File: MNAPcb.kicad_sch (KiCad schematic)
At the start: 10 parts, among them J1 STLINK/V2, J2 DA15_Socket, J3 USB_C_Receptacle_USB2.0_16P, J4 Conn_Coaxial, J5 SineWaveIn1, J6 SineWaveIn, J7 Conn_01x02

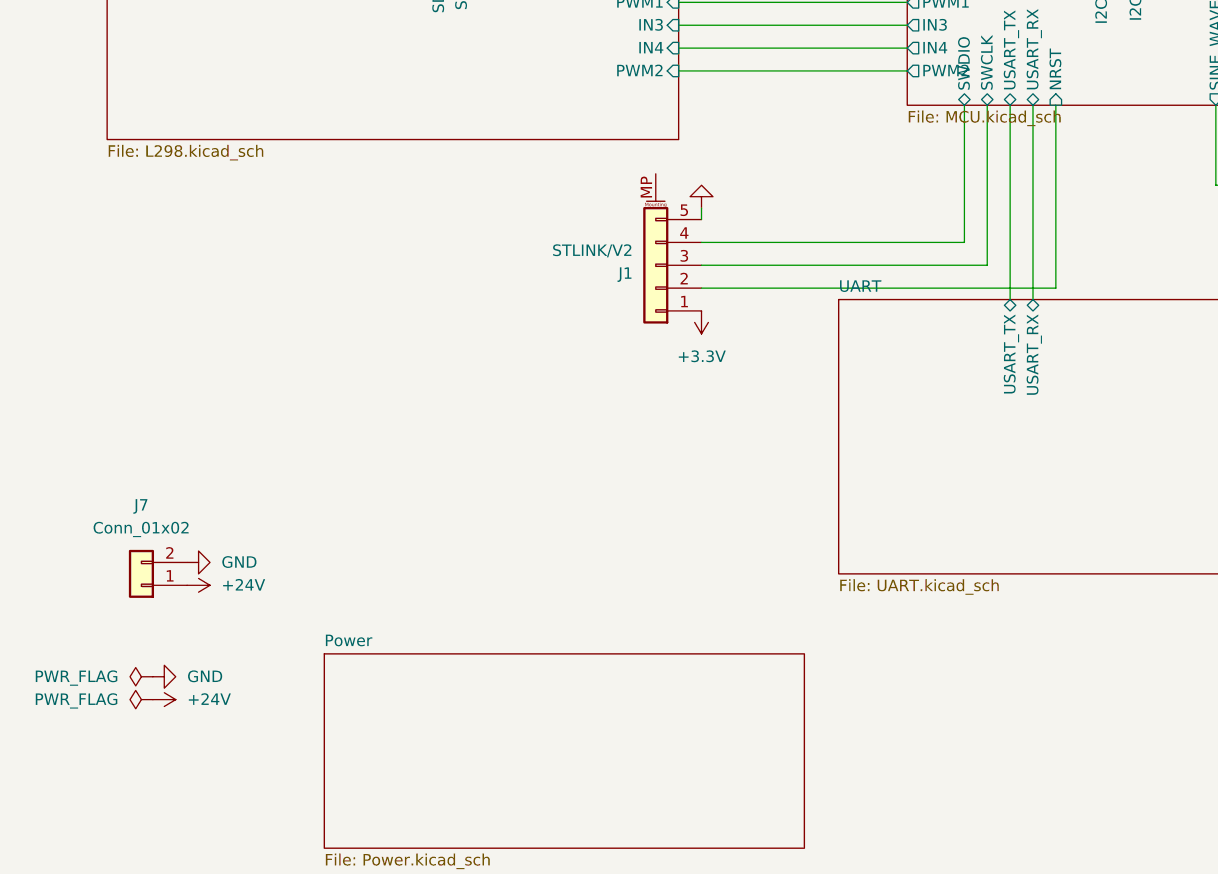
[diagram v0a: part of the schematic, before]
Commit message: Added Footprint
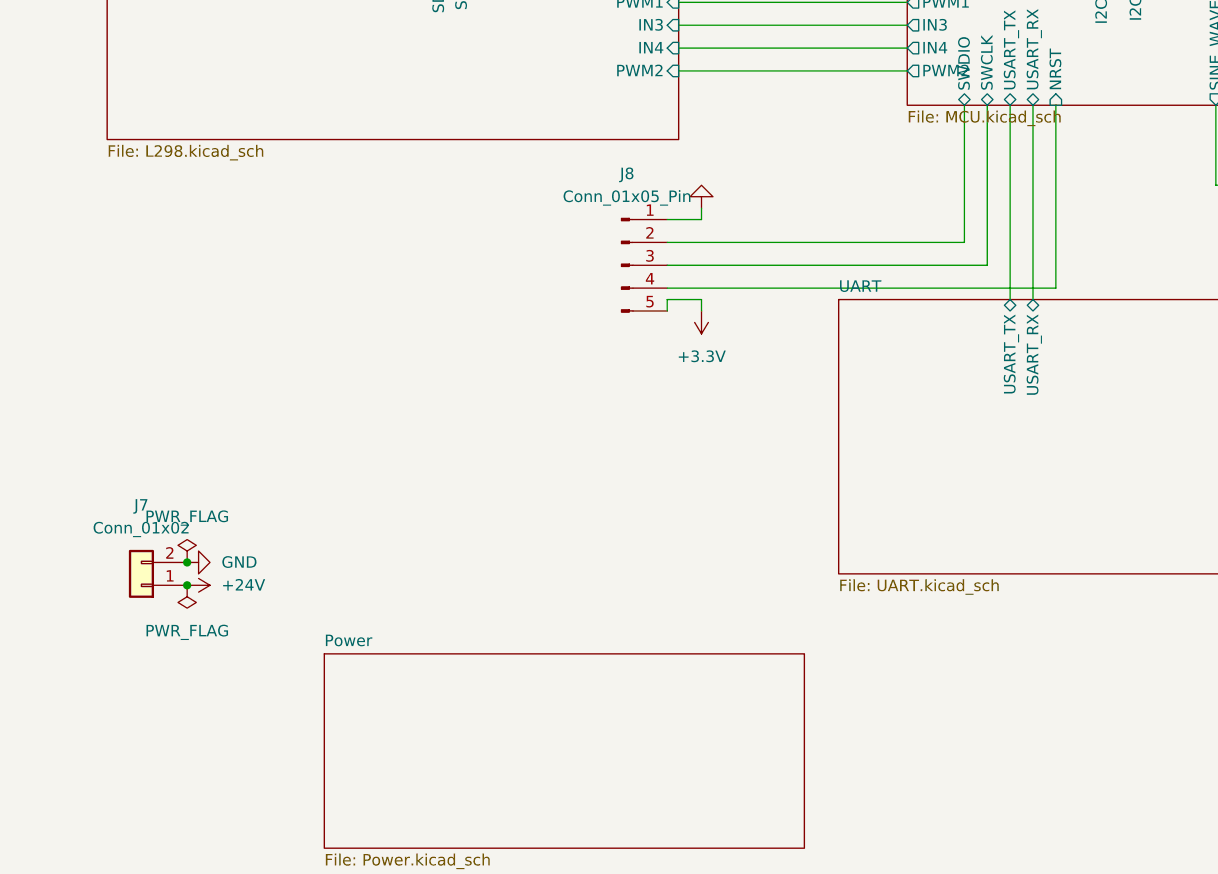
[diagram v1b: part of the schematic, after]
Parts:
- removed J1: STLINK/V2, symbol Connector_Generic_MountingPin:Conn_01x05_MountingPin
- added J8: Conn_01x05_Pin, Connector_PinHeader_2.54mm:PinHeader_1x05_P2.54mm_Vertical_SMD_Pin1Left, symbol Connector:Conn_01x05_Pin
- C17: footprint (none) -> Capacitor_SMD:C_0805_2012Metric_Pad1.18x1.45mm_HandSolder
- J3: footprint (none) -> Connector_USB:USB_C_Receptacle_HRO_TYPE-C-31-M-12
- R10, R7: footprint (none) -> Resistor_SMD:R_0805_2012Metric_Pad1.20x1.40mm_HandSolder
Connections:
- net +3.3V: now also J8.5 (Pin_5)
- net GND: now also J8.1 (Pin_1)
- net MCU/NRST: now also J8.4 (Pin_4)
- net MCU/SWCLK: now also J8.3 (Pin_3)
- net MCU/SWDIO: now also J8.2 (Pin_2)

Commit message: Added a Relay Circuit
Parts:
- added J1: DA15_Socket, Connector_Dsub:DSUB-15_Socket_Horizontal_P2.77x2.54mm_EdgePinOffset9.40mm, symbol Connector:DA15_Socket
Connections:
- no-connect marks 8 -> 14
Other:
- added sheet RelayControl (RelayControl.kicad_sch)
- sheet MCU ports: added K1IN, K2IN, K3IN, K4IN; removed none
- moved on the sheet: J4, J5, J6

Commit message: Solved errors
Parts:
- removed J1: DA15_Socket, Connector_Dsub:DSUB-15_Socket_Horizontal_P2.77x2.54mm_EdgePinOffset9.40mm, symbol Connector:DA15_Socket
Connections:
- net RelayControl/K1OUT: now also J2.6
- net RelayControl/K2OUT: now also J2.15 (P15)
- net RelayControl/K3OUT: now also J2.14 (P14)
- net RelayControl/K4OUT: now also J2.13 (P13)
- no-connect marks 14 -> 4
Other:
- sheet RelayControl ports: added none; removed SCL_RELAY, SDA_RELAY

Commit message: New PCB Changes
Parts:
- J7: footprint (none) -> Connector_TE-Connectivity:TE_826576-2_1x02_P3.96mm_Vertical
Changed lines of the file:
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@@
 			)
 		)
-		(property "Footprint" ""
+		(property "Footprint" "Connector_TE-Connectivity:TE_826576-2_1x02_P3.96mm_Vertical"
 			(at 19.05 138.43 0)
 			(effects

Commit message: FInal Changes in Schgematic
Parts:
- removed J5: SineWaveIn1, Connector_Coaxial:SMA_Amphenol_132289_EdgeMount, symbol Connector:Conn_Coaxial
- added H1, H2, H3, H4: MountingHole, MountingHole:MountingHole_3.2mm_M3_DIN965, symbol Mechanical:MountingHole
- added J1: Conn_01x03_Pin, Connector_Molex:Molex_KK-254_AE-6410-03A_1x03_P2.54mm_Vertical, symbol Connector:Conn_01x03_Pin
- added J5, J9: Conn_01x02, Connector_TE-Connectivity:TE_826576-2_1x02_P3.96mm_Vertical, symbol Connector_Generic:Conn_01x02
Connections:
- net GND: now also J1.2 (Pin_2), J5.1 (Pin_1), J9.1 (Pin_1)
- net +3.3V: no longer names the net of J8.5 (Pin_5)
- new net +12: J5.2 (Pin_2)
- new net +15: J1.1 (Pin_1)
- new net +24: J9.2 (Pin_2)
- new net -15V: J1.3 (Pin_3)
- no-connect marks 4 -> 5
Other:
- added sheet CurrentTracking (untitled.kicad_sch)
- sheet L298 ports: added none; removed SCL_MOTOR, SDA_MOTOR

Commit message: Fixed the Silkscreen issue
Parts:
- J3: footprint Connector_USB:USB_C_Receptacle_HRO_TYPE-C-31-M-12 -> Connector_USB:USB_C_Receptacle_GCT_USB4085
- J8: footprint Connector_PinHeader_2.54mm:PinHeader_1x05_P2.54mm_Vertical_SMD_Pin1Left -> Connector_PinHeader_2.54mm:PinHeader_1x05_P2.54mm_Vertical
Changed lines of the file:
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@@
 			)
 		)
-		(property "Footprint" "Connector_USB:USB_C_Receptacle_HRO_TYPE-C-31-M-12"
+		(property "Footprint" "Connector_USB:USB_C_Receptacle_GCT_USB4085"
 			(at 219.71 120.65 0)
 			(effects
@@
 			)
 		)
-		(property "Footprint" "Connector_PinHeader_2.54mm:PinHeader_1x05_P2.54mm_Vertical_SMD_Pin1Left"
+		(property "Footprint" "Connector_PinHeader_2.54mm:PinHeader_1x05_P2.54mm_Vertical"
 			(at 72.39 102.87 0)
 			(effects

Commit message: Deleted Uneeded Portion
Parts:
- removed J4: Conn_Coaxial, Connector_Coaxial:SMA_Amphenol_132289_EdgeMount, symbol Connector:Conn_Coaxial
- removed J6: SineWaveIn, Connector_Coaxial:SMA_Amphenol_132289_EdgeMount, symbol Connector:Conn_Coaxial
- removed J8: Conn_01x05_Pin, Connector_PinHeader_2.54mm:PinHeader_1x05_P2.54mm_Vertical, symbol Connector:Conn_01x05_Pin
- added J8: Conn_01x04_Pin, Connector_JST:JST_EH_B4B-EH-A_1x04_P2.50mm_Vertical, symbol Connector:Conn_01x04_Pin
- J3: footprint Connector_USB:USB_C_Receptacle_GCT_USB4085 -> Connector_USB:USB_C_Receptacle_G-Switch_GT-USB-7010ASV
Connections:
- net RelayControl/K2OUT is gone; now on net ADC/POT2_V: J2.15 (P15)
- net +12: now also J2.8
- net ADC/POT1_V: now also J2.7; no longer J2.5
- net ADC/POT2_V: no longer J2.12 (P12)
- net GND: now also J8.4 (Pin_4)
- net MCU/NRST: now also J8.1 (Pin_1)
- net MCU/SWCLK: now also J8.2 (Pin_2)
- net MCU/SWDIO: now also J8.3 (Pin_3)
- net +12V: no longer names the net of J2.4
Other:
- sheet ADC ports: added none; removed ADC2, SineWaveIn
- sheet MCU ports: added none; removed ADC2, SINE_WAVE

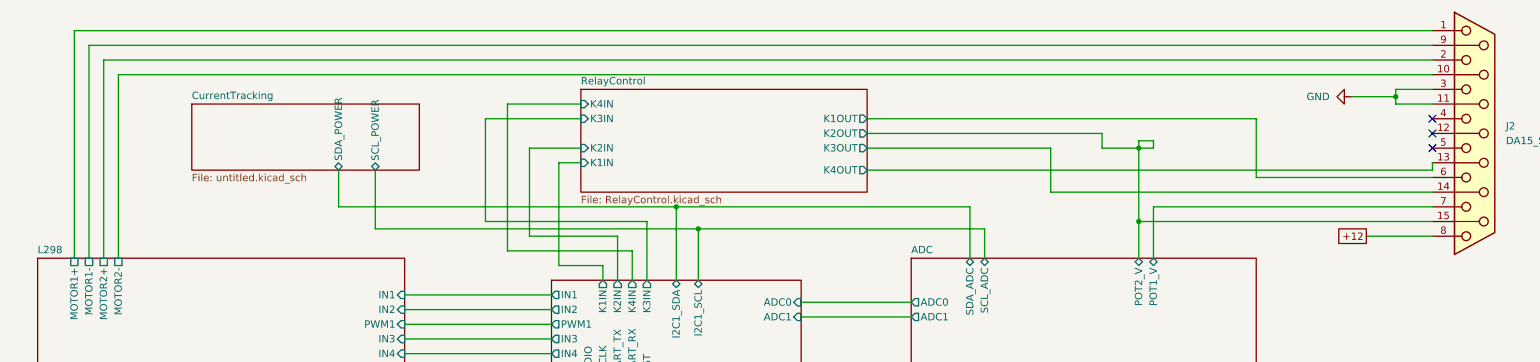
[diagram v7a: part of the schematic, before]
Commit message: Used Zones and Net
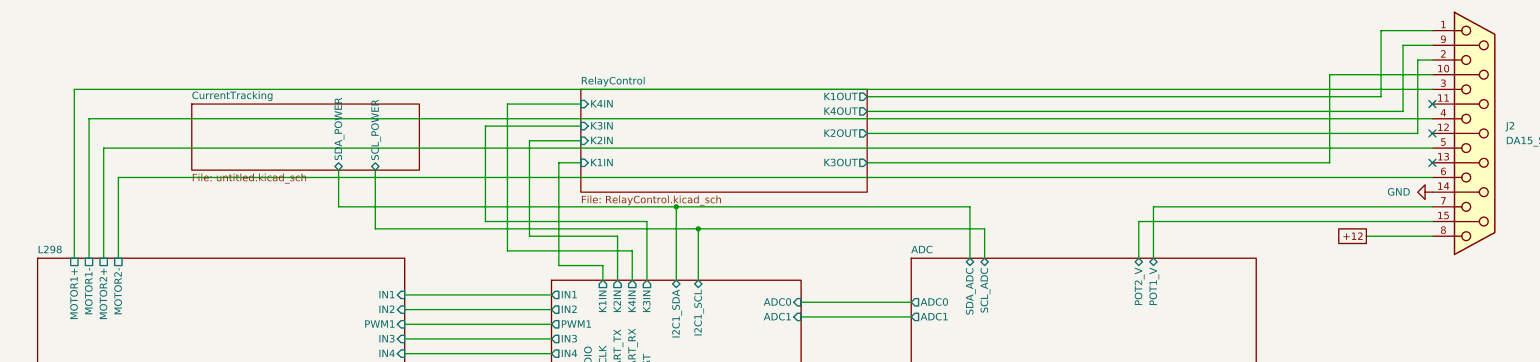
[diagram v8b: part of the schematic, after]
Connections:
- net GND: now also J2.14 (P14); no longer J2.11 (P111), J2.3
- net L298/MOTOR1+: now also J2.3; no longer J2.1
- net L298/MOTOR1-: now also J2.4; no longer J2.9 (P9)
- net L298/MOTOR2+: now also J2.5; no longer J2.2
- net L298/MOTOR2-: now also J2.6; no longer J2.10 (P10)
- net RelayControl/K1OUT: now also J2.1; no longer J2.6
- net RelayControl/K3OUT: now also J2.10 (P10); no longer J2.14 (P14)
- net RelayControl/K4OUT: now also J2.9 (P9); no longer J2.13 (P13)
- new net RelayControl/K2OUT: J2.2
